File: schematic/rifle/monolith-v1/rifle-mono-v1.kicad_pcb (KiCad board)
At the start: 2 copper layers, 100 x 30 mm, 79 parts, among them P1 MICROSD-SDIO-CD, P10 RC522, P11 Speaker1, P12 Speaker2, P13 I2C display, P14 I2C display, P15 FLASH, P16 VIBRO, P17 IR_LED, P18 USB_OTG, P19 GND, P2 SWD, P3 G B Vcc, P4 NRF24L01, P5 USB_A, P6 S_A_M1_M2, P7 DEBUG_TX, P8 Fire, P9 Reload, Q1 IRLML6402, Q2 IRLML2502, Q3 IRLML2502, Q4 IRLML2502, Q5 IRLML2502, Q6 IRLML2502, Q7 IRLML2502, U1 STM32F103RE, U2 USBLC6-4, U3 MCP73831, U4 NCP551, U5 PAM8403, Y1 8MHz

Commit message: [PCB[ Rifle mono silk in process
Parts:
- moved C3 1.14 mm to (65.9, 32.1)
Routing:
- net GND: track 92.5 -> 133.2 mm, vias 22 -> 31
- net +3V3: track 163.5 -> 193.1 mm, vias 10 -> 12
- net (no net): vias 0 -> 8
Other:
- net class Default: trace_width 0.4 -> 0.25

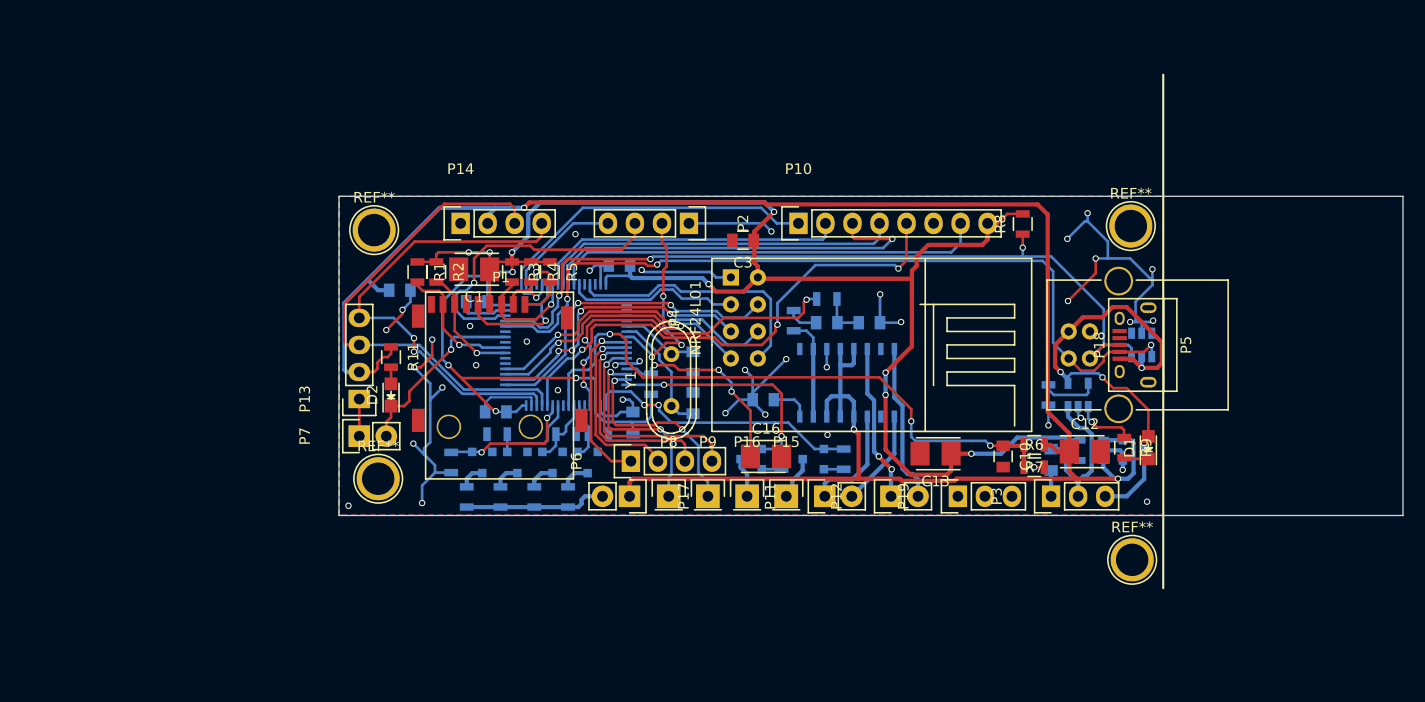
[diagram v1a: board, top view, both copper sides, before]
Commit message: [PCB] [firmware] Rifle monolith pcb final. Firmware build fix
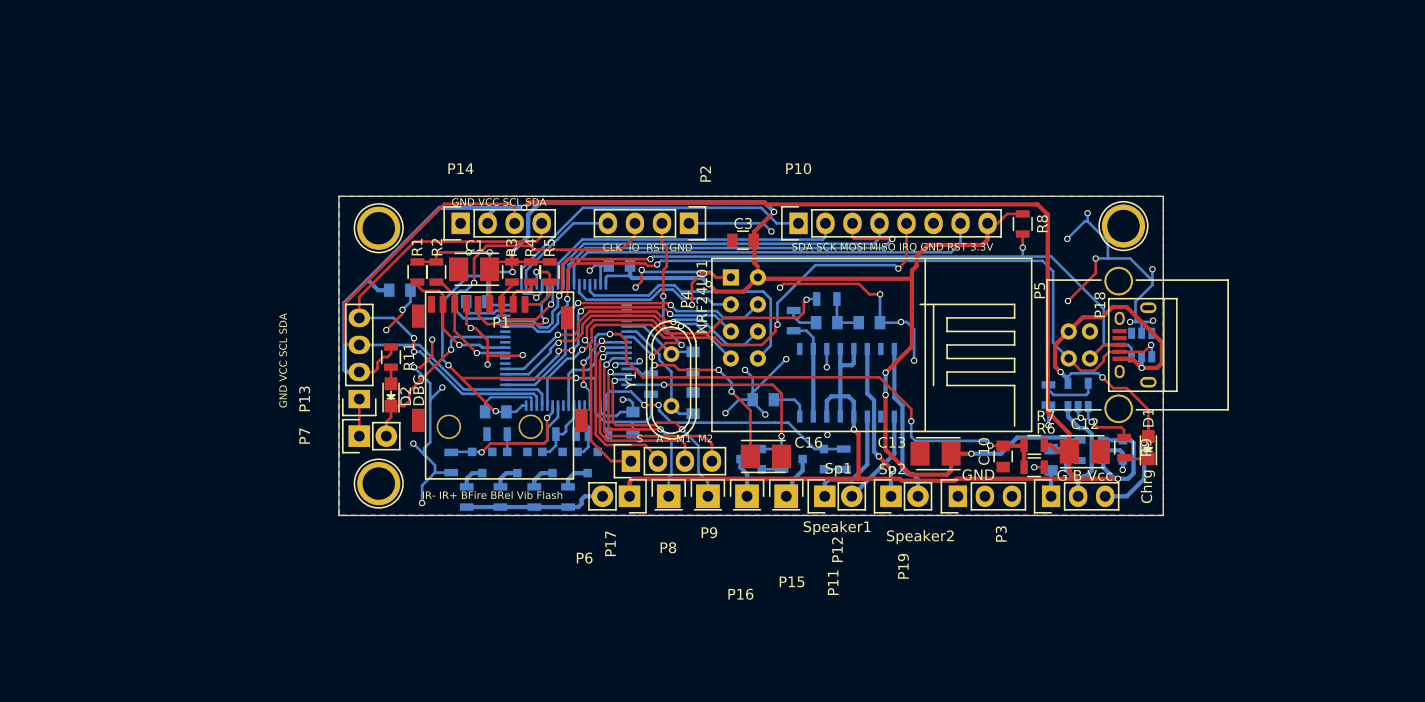
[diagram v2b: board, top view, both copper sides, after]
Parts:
- removed the REF** at (102.5, 62.1)
- U2: value USBLC6-4 -> USBLC6
- moved REF** 0.69 mm to (101.7, 30.7)
- moved REF** 0.47 mm to (31.7, 30.9)
- moved REF** 0.46 mm to (31.7, 54.9)
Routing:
- net GND: track 133.2 -> 165.8 mm, vias 31 -> 38
- net +3V3: track 193.1 -> 197.0 mm
- net (no net): vias 8 -> 1
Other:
- board size 100 x 30 mm -> 77.5 x 30 mm
- board text added: "CLK IO RST GND"
- board text added: "Caustic Lasertag System Rifle board m rev. 1.0"
- board text added: "GND VCC SCL SDA"
- board text added: "IR- IR+ BFire BRel Vib Flash"
- board text added: "S A M1 M2"
- board text added: "SDA SCK MOSI MISO IRQ GND RST 3.3V"
- board text added: "Sp1"
- board text added: "Sp2"

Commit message: [pcb] Rifle monolithic panelized done and send to factory
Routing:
- net +3V3: track 197.0 -> 195.7 mm, vias 12 -> 11

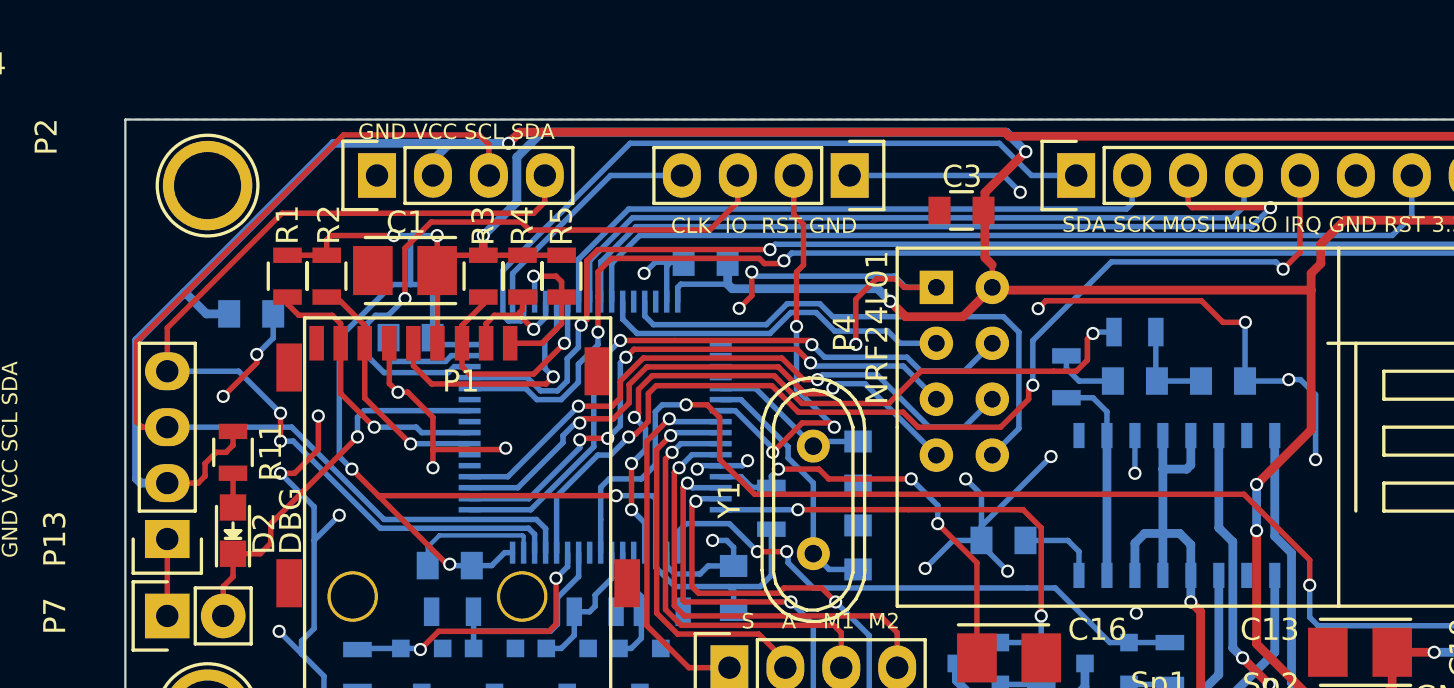
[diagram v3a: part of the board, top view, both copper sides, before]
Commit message: Rifle mono board 1.1: capacitor near PAM; I2C pull-up; Laser TTL output
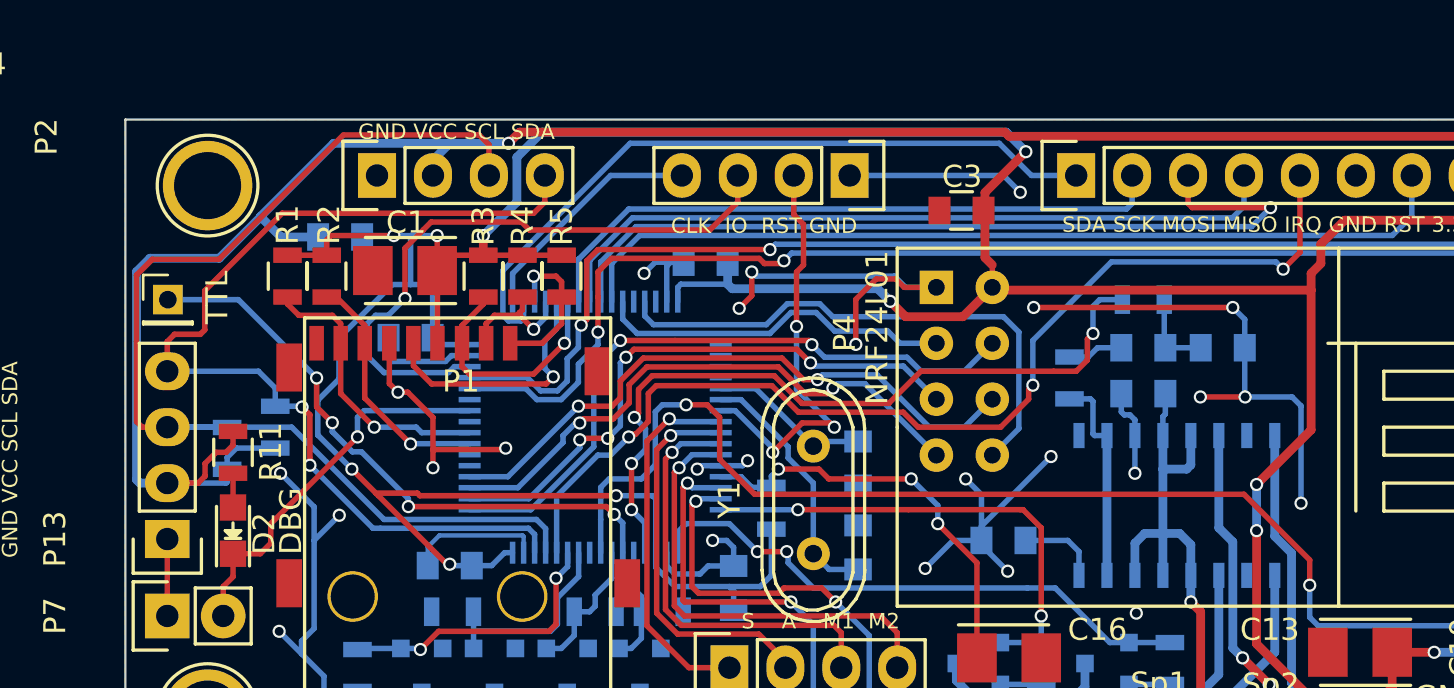
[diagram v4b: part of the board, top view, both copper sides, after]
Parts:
- added C8: 0.1, Capacitors_SMD:C_0805, B.Cu at (74.2, 40.4)
- added P20: TTL, Pin_Headers:Pin_Header_Straight_1x01_Pitch2.00mm, F.Cu at (29.9, 36.1)
- added R25: 3.3k, Resistors_SMD:R_0805, B.Cu at (34.7, 41.9)
- added R26: 3.3k, Resistors_SMD:R_0805, B.Cu at (32.6, 42.9)
- U2: value USBLC6 -> USBLC6-4
- moved C11 5.34 mm to (37.7, 33.3)
- moved C19 1.56 mm to (74.2, 38.3)
- moved R13 1.52 mm to (74.2, 36.1)
- moved C18 1.51 mm to (77.8, 38.3)
- moved R14 0.15 mm to (70.8, 39.7)
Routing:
- net /IR_CH1: track 5.44 -> 32.9 mm, vias 0 -> 4
- net VCC: track 194.1 -> 204.7 mm
- net I2C_SCL: track 46.8 -> 51.3 mm
- net GND: track 165.7 -> 163.1 mm, vias 38 -> 36
- net DAC_OUT: track 32.5 -> 34.3 mm
- net I2C_SDA: track 44.0 -> 45.8 mm
- net +3V3: track 195.7 -> 196.7 mm
- net Net-(C18-Pad2): track 4.31 -> 3.81 mm
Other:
- net class Default: trace_width 0.25 -> 0.254
- board text added: "Caustic Lasertag System Rifle board m rev. 1.1"
- board text removed: "Caustic Lasertag System Rifle board m rev. 1.0"

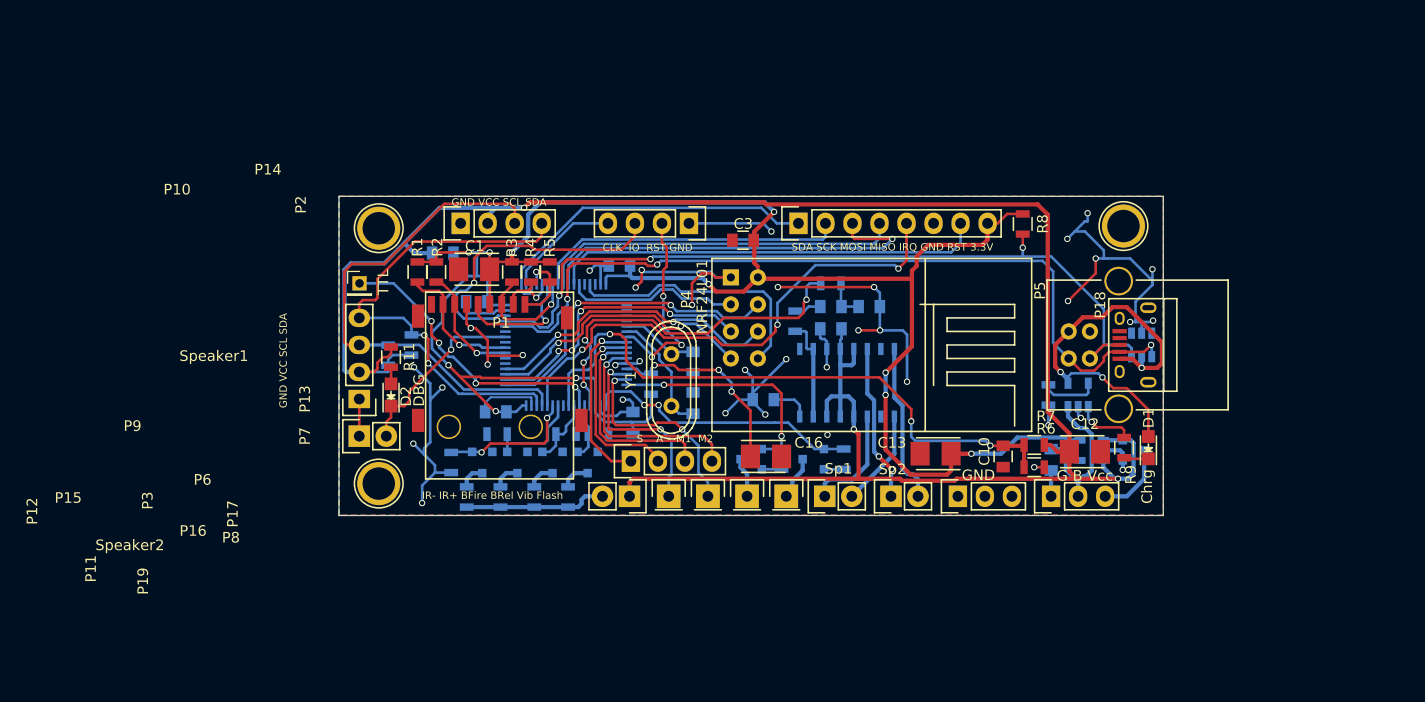
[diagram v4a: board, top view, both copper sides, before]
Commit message: [pcb] Group board rifle+smart sensors ordered
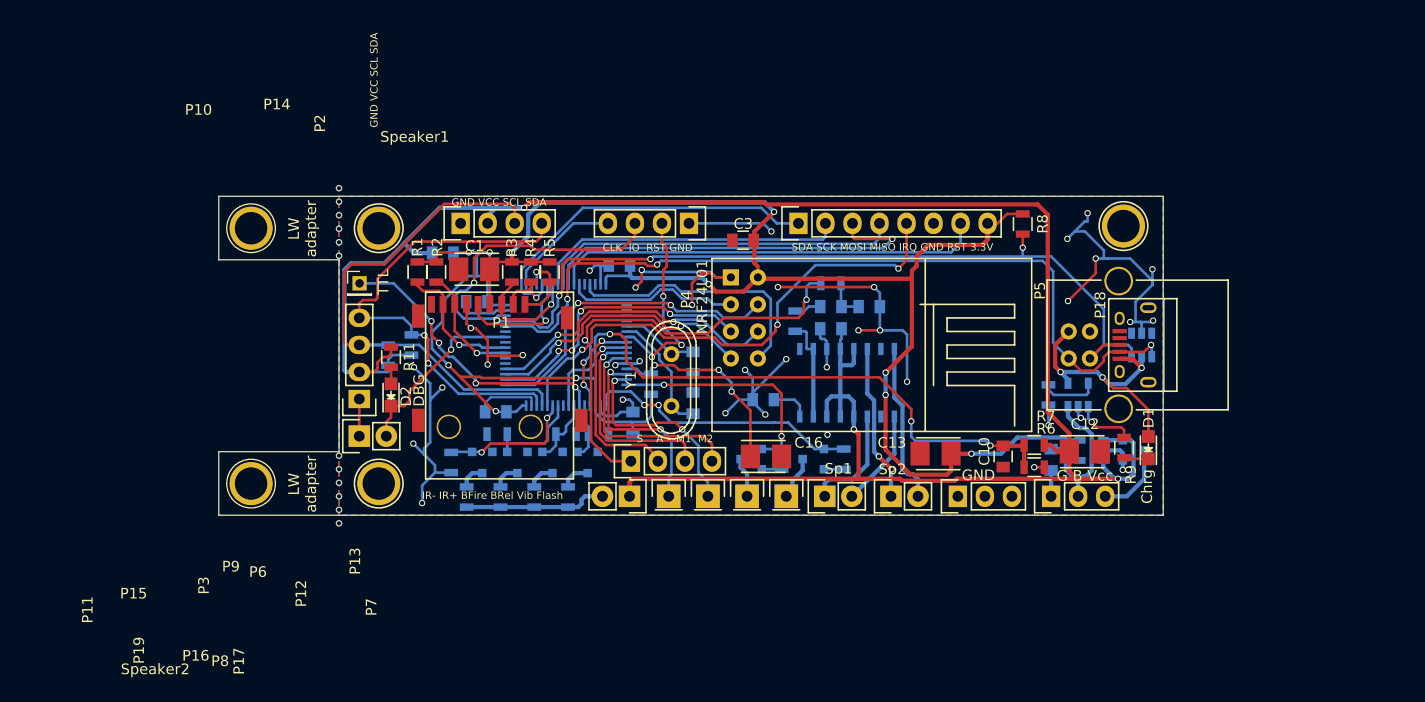
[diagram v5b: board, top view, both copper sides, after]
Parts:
- added REF**: 1pin, Connect:1pin, F.Cu at (19.7, 30.9)
- added REF**: 1pin, Connect:1pin, F.Cu at (19.7, 54.9)
- added wholes: WHOLES-LINE-3, components:wholes-line-3, F.Cu at (27.9, 28.4)
- added wholes: WHOLES-LINE-3, components:wholes-line-3, F.Cu at (27.9, 32.3)
- added wholes: WHOLES-LINE-3, components:wholes-line-3, F.Cu at (27.9, 53.6)
- added wholes: WHOLES-LINE-3, components:wholes-line-3, F.Cu at (27.9, 57.4)
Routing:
- net Net-(D1-Pad2): track 36.7 -> 26.2 mm
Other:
- board size 77.5 x 30 mm -> 88.8 x 30 mm
- net class Default: trace_width 0.254 -> 0.4
- board text added: "LW adapter"
